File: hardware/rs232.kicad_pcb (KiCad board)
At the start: 2 copper layers, 45 x 35 mm, 36 parts, among them J1 DB9, P1 CON-SENSOR, P2 CONN_5, P3 CONN_5, P4 BOOT, U1 XMC1XXX48, U3 SP3232EBCN, U4 DRILL, U5 DRILL, U6 DRILL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

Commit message: Minor adjustments
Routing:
- net GND: track 43.3 -> 38.5 mm, vias 13 -> 14
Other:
- board text added: "RS232 2.0"
- board text removed: "RS232 1.0"
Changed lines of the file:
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@@
     (links 76)
     (no_connects 0)
-    (area 125.109499 82.909499 170.490501 118.290501)
+    (area 12.604132 82.245139 171.154861 196.040743)
     (thickness 1.6002)
     (drawings 23)
-    (tracks 347)
+    (tracks 346)
     (zones 0)
     (modules 36)
@@
   (page A4)
   (title_block
-    (title "Serial Bricklet")
-    (date "5 mar 2015")
+    (title "RS232 Bricklet 2.0")
+    (date 2018-01-16)
     (rev 1.0)
     (company "Tinkerforge GmbH")
     (comment 1 "Licensed under CERN OHL v.1.1")
-    (comment 2 "Copyright (©) 2015, B.Nordmeyer <bastian@tinkerforge.com>")
+    (comment 2 "Copyright (©) 2018, L.Lauer <lukas@tinkerforge.com>")
   )
   (layers
@@
   )
   (setup
-    (last_trace_width 0.2)
+    (last_trace_width 0.249)
     (user_trace_width 0.2)
     (user_trace_width 0.25)
@@
     (effects (font (size 0.8001 0.8001) (thickness 0.14986)))
   )
-  (gr_text "RS232\n1.0" (at 128.7 109.6 180) (layer F.SilkS)
+  (gr_text "RS232\n2.0" (at 128.7 109.6 180) (layer F.SilkS)
     (effects (font (size 0.8001 0.8001) (thickness 0.14986)))
   )
+  (via (at 142.6 99.4) (size 0.70104) (drill 0.24892) (layers Vorderseite Rückseite) (net 1) (status C00000))
   (segment (start 168.6 101.45) (end 168.6 100.6) (width 0.2) (layer Vorderseite) (net 1))
   (via (at 168.6 100.6) (size 0.55) (drill 0.25) (layers Vorderseite Rückseite) (net 1))
@@
   (segment (start 135.05 100.78) (end 135.05 99.30992) (width 0.55) (layer Vorderseite) (net 1))
   (segment (start 135.05 99.30992) (end 134.9999 99.25982) (width 0.55) (layer Vorderseite) (net 1))
-  (segment (start 138.99066 96.65172) (end 139.85172 96.65172) (width 0.2) (layer Vorderseite) (net 1))
-  (segment (start 139.85172 96.65172) (end 142.6 99.4) (width 0.2) (layer Vorderseite) (net 1))
   (segment (start 134.9999 100.7299) (end 135.05 100.78) (width 0.2) (layer Vorderseite) (net 1))
   (segment (start 136.6001 95.5401) (end 136.55 95.49) (width 0.2) (layer Vorderseite) (net 1))

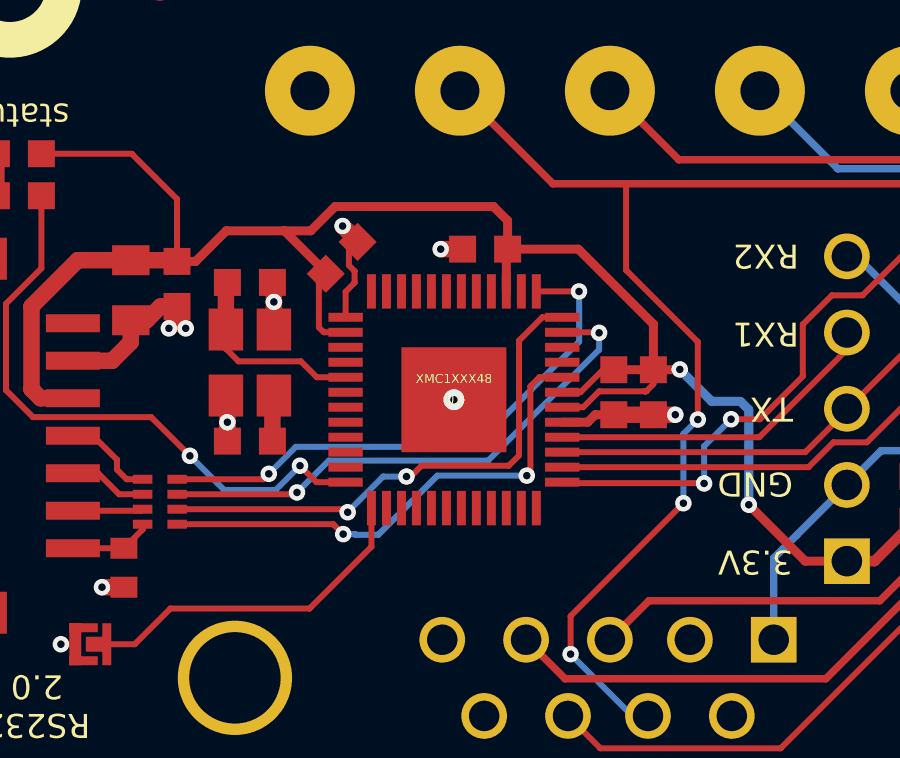
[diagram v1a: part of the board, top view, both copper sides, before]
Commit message: remove 0 ohm resitor in crystal circuitry
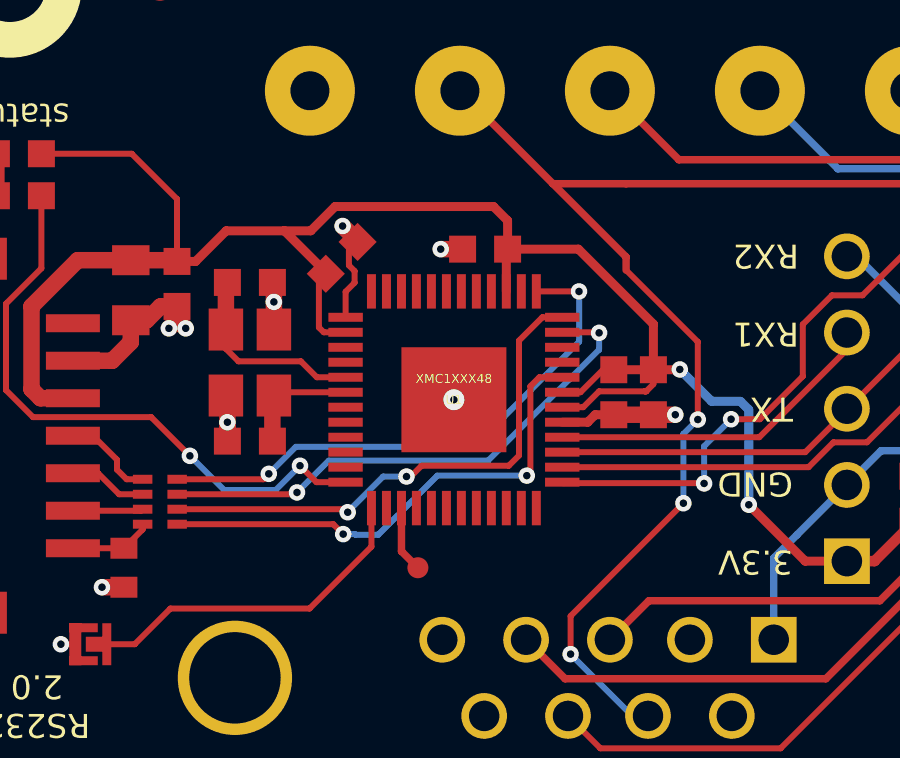
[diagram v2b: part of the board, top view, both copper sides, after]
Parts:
- added P5: BOOT, kicad-libraries:DEBUG_PAD, F.Cu at (141.4, 105.0)
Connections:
- J1 pad 2: Net-(J1-Pad2) -> (no net)
- J1 pad 5: Net-(J1-Pad5) -> (no net)
- J1 pad 6: Net-(J1-Pad6) -> (no net)
- J1 pad 9: Net-(J1-Pad9) -> (no net)
- P1 pad 1: Net-(P1-Pad1) -> (no net)
- U1 pad 10: Net-(U1-Pad10) -> (no net)
- U1 pad 11: Net-(U1-Pad11) -> (no net)
- U1 pad 12: Net-(U1-Pad12) -> (no net)
- U1 pad 2: Net-(U1-Pad2) -> (no net)
- U1 pad 21: Net-(U1-Pad21) -> (no net)
- U1 pad 22: Net-(U1-Pad22) -> (no net)
- U1 pad 26: Net-(U1-Pad26) -> (no net)
- U1 pad 28: Net-(U1-Pad28) -> (no net)
- U1 pad 29: Net-(U1-Pad29) -> (no net)
- U1 pad 30: Net-(U1-Pad30) -> (no net)
- U1 pad 31: Net-(U1-Pad31) -> (no net)
- U1 pad 32: Net-(U1-Pad32) -> (no net)
- U1 pad 33: Net-(U1-Pad33) -> (no net)
- U1 pad 34: Net-(U1-Pad34) -> (no net)
- U1 pad 35: Net-(U1-Pad35) -> (no net)
- U1 pad 36: Net-(U1-Pad36) -> (no net)
- U1 pad 39: Net-(U1-Pad39) -> (no net)
- U1 pad 4: Net-(U1-Pad4) -> (no net)
- U1 pad 40: Net-(U1-Pad40) -> (no net)
- U1 pad 42: Net-(R1-Pad1) -> Net-(C5-Pad2)
- U1 pad 43: Net-(U1-Pad43) -> (no net)
- U1 pad 44: Net-(U1-Pad44) -> (no net)
- U1 pad 45: Net-(U1-Pad45) -> (no net)
- U1 pad 46: Net-(U1-Pad46) -> (no net)
- U1 pad 47: Net-(U1-Pad47) -> (no net)
- U1 pad 5: Net-(U1-Pad5) -> (no net)
- U1 pad 6: Net-(U1-Pad6) -> (no net)
- U1 pad 7: Net-(U1-Pad7) -> (no net)
- U1 pad 8: Net-(U1-Pad8) -> (no net)
- U1 pad 9: Net-(U1-Pad9) -> (no net)
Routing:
- net Net-(C5-Pad2): track 1.61 -> 4.04 mm
- net Net-(P5-Pad1): track 0.00 -> 2.21 mm
- net Net-(J1-Pad7): track 46.9 -> 47.9 mm

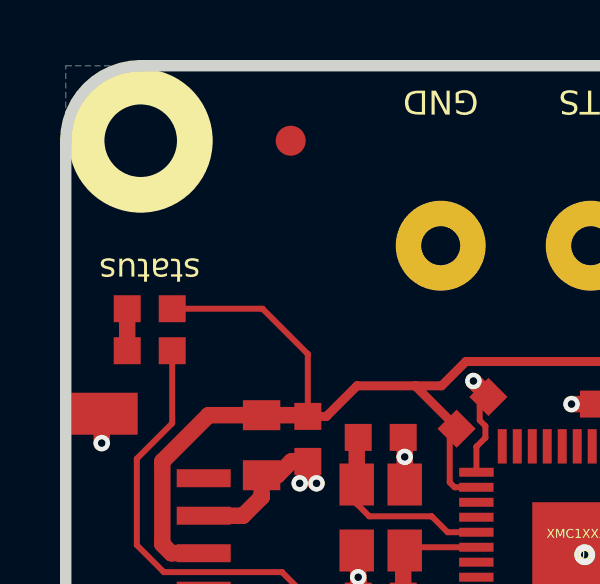
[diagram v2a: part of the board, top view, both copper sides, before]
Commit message: fix status text
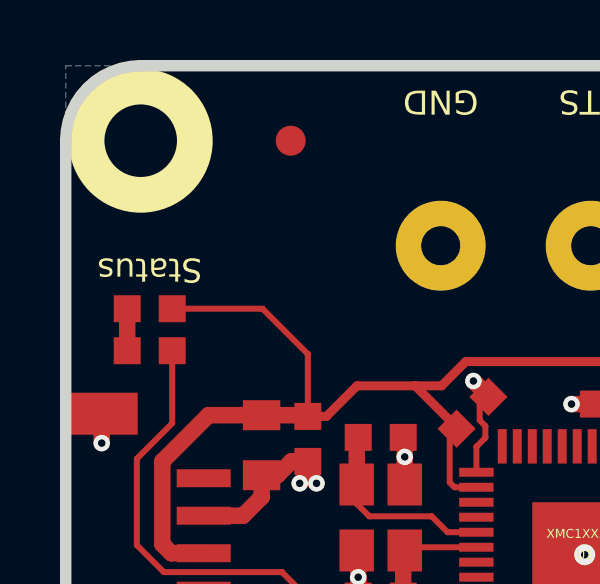
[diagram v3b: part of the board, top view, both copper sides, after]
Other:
- board text added: "Status"
- board text removed: "status"
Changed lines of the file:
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@@
     (links 78)
     (no_connects 0)
-    (area 125.109499 82.909499 170.490501 118.290501)
+    (area 12.704144 82.245139 171.154861 196.440793)
     (thickness 1.6002)
     (drawings 23)
@@
   )
   (setup
-    (last_trace_width 0.2)
+    (last_trace_width 0.249)
     (user_trace_width 0.2)
     (user_trace_width 0.25)
@@
       (net 31 "Net-(P5-Pad1)"))
   )
-  (gr_text status (at 128.1 89.9 180) (layer F.SilkS)
+  (gr_text Status (at 128.1 89.9 180) (layer F.SilkS)
     (effects (font (size 0.8 0.8) (thickness 0.15)))
   )
